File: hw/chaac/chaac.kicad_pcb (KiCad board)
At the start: 2 copper layers, 42 x 55 mm, 56 parts, among them J1 Battery, J2 TC2030-CTX, J3 UART, J4 windrain, Q1 Q_PMOS_GSD, SW1 RST, SW2 RST, U1 TPS7A0530PDBVT, U2 NRF52811-QFAA, U3 BMP280, U4 SHT3x-DIS, U5 E22-X00M22S, Y2 32.768kHz

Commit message: Adding chaac v5.0
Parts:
- removed the C14 at (117.5, 152.5)
- removed C16: 0.1uF, Capacitor_SMD:C_0603_1608Metric
- removed the R14 at (132.0, 168.0)
- removed the REF** at (124.4, 151.0)
- removed the REF** at (141.0, 133.0)
- removed the REF** at (107.0, 133.0)
- removed SW1, SW2: RST, alvarop:PTS820J25MSMTRLFS
- removed the U3 at (137.3, 146.0)
- added C2: 10uF, Resistor_SMD:R_0603_1608Metric, F.Cu at (116.6, 162.5)
- added C21: 0.1uF, Capacitor_SMD:C_0402_1005Metric, F.Cu at (141.2, 157.4)
- added C3: 4.7uF, Capacitor_SMD:C_0402_1005Metric, F.Cu at (119.6, 164.3)
- added C7: 0.1uF, Capacitor_SMD:C_0402_1005Metric, F.Cu at (142.0, 138.3)
- added C8: 4.7uF, Capacitor_SMD:C_0402_1005Metric, F.Cu at (122.8, 157.7)
- added D1: RB521CS30L,315, alvarop:RB521CS30L, F.Cu at (115.2, 168.7)
- added D2: LED_ALT, LED_SMD:LED_0603_1608Metric, F.Cu at (132.3, 159.7)
- added D3: LED_ALT, LED_SMD:LED_0603_1608Metric, F.Cu at (129.3, 159.7)
- added D4: LED_ALT, LED_SMD:LED_0603_1608Metric, F.Cu at (130.8, 159.7)
- added G***: LOGO, alvarop:weather_station, B.Cu at (115.0, 156.0)
- added J2: Battery, alvarop:S2B-PH-SM4-TB, F.Cu at (108.0, 142.0)
- added R1: 270k, Resistor_SMD:R_0402_1005Metric, F.Cu at (124.3, 165.2)
- added R10: 10k, Resistor_SMD:R_0402_1005Metric, F.Cu at (131.8, 164.2)
- added R11: 10k, Resistor_SMD:R_0402_1005Metric, F.Cu at (126.3, 165.7)
- added R12: 10k, Resistor_SMD:R_0402_1005Metric, F.Cu at (129.8, 164.2)
- added R13: 10k, Resistor_SMD:R_0402_1005Metric, F.Cu at (130.8, 164.2)
- added R20: 10k, Resistor_SMD:R_0402_1005Metric, F.Cu at (130.0, 171.3)
- added R4: 1M, Resistor_SMD:R_0402_1005Metric, F.Cu at (142.3, 167.1)
- added R5: 100k, Resistor_SMD:R_0402_1005Metric, F.Cu at (124.8, 157.7)
- added REF**: OSHW-Logo2_7.3x6mm_SilkScreen, Symbol:OSHW-Logo2_7.3x6mm_SilkScreen, F.Cu at (139.7, 151.9)
- added U2: MCP73871, alvarop:MCP73871, F.Cu at (124.8, 161.7)
- added U5: SHT3x-DIS, alvarop:SHT3x, F.Cu at (138.6, 157.4)
- C1: value 1uF -> 100uF; footprint Capacitor_SMD:C_0603_1608Metric -> Capacitor_SMD:CP_Elec_6.3x5.4
- C18: renamed from C17; footprint Capacitor_SMD:C_0603_1608Metric -> Capacitor_SMD:C_0402_1005Metric
- C19: renamed from C18; footprint Capacitor_SMD:C_0603_1608Metric -> Capacitor_SMD:C_0402_1005Metric
- C20: renamed from C15; footprint Capacitor_SMD:C_0603_1608Metric -> Capacitor_SMD:C_0402_1005Metric
- C22: renamed from C21; footprint Capacitor_SMD:C_0603_1608Metric -> Capacitor_SMD:C_0402_1005Metric
- C23: renamed from C22; footprint Capacitor_SMD:C_0603_1608Metric -> Capacitor_SMD:C_0402_1005Metric
- C24: renamed from C19; footprint Capacitor_SMD:C_0603_1608Metric -> Capacitor_SMD:C_0402_1005Metric
- C25: renamed from C20; footprint Capacitor_SMD:C_0603_1608Metric -> Capacitor_SMD:C_0402_1005Metric
- C5: renamed from C2; footprint Capacitor_SMD:C_0603_1608Metric -> Capacitor_SMD:C_0402_1005Metric
- C6: renamed from C7; footprint Capacitor_SMD:C_0603_1608Metric -> Capacitor_SMD:C_0402_1005Metric
- J1: value Battery -> Solar
- J3: footprint Connector_PinHeader_2.54mm:PinHeader_1x03_P2.54mm_Vertical -> Connector_PinHeader_2.54mm:PinHeader_1x02_P2.54mm_Vertical
- R14: renamed from R3; footprint Resistor_SMD:R_0603_1608Metric -> Resistor_SMD:R_0402_1005Metric
- R15: renamed from R4; footprint Resistor_SMD:R_0603_1608Metric -> Resistor_SMD:R_0402_1005Metric
- R16: renamed from R10; value 1k -> 0; footprint Resistor_SMD:R_0603_1608Metric -> Resistor_SMD:R_0402_1005Metric
- R17: renamed from R11; footprint Resistor_SMD:R_0603_1608Metric -> Resistor_SMD:R_0402_1005Metric
- R18: renamed from R12; footprint Resistor_SMD:R_0603_1608Metric -> Resistor_SMD:R_0402_1005Metric
- R19: renamed from R13; footprint Resistor_SMD:R_0603_1608Metric -> Resistor_SMD:R_0402_1005Metric
- R2: footprint Resistor_SMD:R_0603_1608Metric -> Resistor_SMD:R_0402_1005Metric
- R21: renamed from R5; footprint Resistor_SMD:R_0603_1608Metric -> Resistor_SMD:R_0402_1005Metric
- R22: renamed from R15; footprint Resistor_SMD:R_0603_1608Metric -> Resistor_SMD:R_0402_1005Metric
- R23: renamed from R16; footprint Resistor_SMD:R_0603_1608Metric -> Resistor_SMD:R_0402_1005Metric
- R3: renamed from R1; value 100k -> 1M; footprint Resistor_SMD:R_0603_1608Metric -> Resistor_SMD:R_0402_1005Metric
- R6, R7: value 4.7k -> 1M; footprint Resistor_SMD:R_0603_1608Metric -> Resistor_SMD:R_0402_1005Metric
- R8: value 0 -> 100k; footprint Resistor_SMD:R_0603_1608Metric -> Resistor_SMD:R_0402_1005Metric
- R9: value 0 -> 1M; footprint Resistor_SMD:R_0603_1608Metric -> Resistor_SMD:R_0402_1005Metric
- U4: value SHT3x-DIS -> DPS368; footprint alvarop:SHT3x -> alvarop:DPS368
- Y1: renamed from Y2; footprint Crystal:Crystal_SMD_3215-2Pin_3.2x1.5mm -> alvarop:ABS05
- moved J4 31.9 mm to (134.8, 131.7), turned to 180 degrees
- moved Q1 26.6 mm to (138.9, 167.9), turned to 0 degrees
- moved R21 21.3 mm to (136.4, 167.5), turned to 270 degrees
- moved U3 21.0 mm to (136.1, 139.3)
- moved R6 21.0 mm to (120.5, 155.2), turned to 90 degrees
- moved L2 20.8 mm to (137.9, 145.1)
- moved C17 20.7 mm to (138.8, 135.1)
- moved C14 20.6 mm to (131.5, 141.0), turned to 270 degrees
- moved C11 20.4 mm to (140.5, 143.0), turned to 90 degrees
- moved C10 20.2 mm to (139.5, 144.0), turned to 90 degrees
- moved Y1 20.1 mm to (141.5, 140.9), turned to 90 degrees
- moved C9 20.0 mm to (135.5, 145.7)
- moved L1 20.0 mm to (136.5, 145.7)
- moved C15 19.9 mm to (142.0, 139.4), turned to 0 degrees
- moved C12 19.6 mm to (132.0, 144.0), turned to 90 degrees
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- renumbered C4 to C10, C5 to C11, C6 to C12, C9 to C13, C11 to C14, C12 to C15, C13 to C17, C3 to C9, D1 to D5, D2 to D6, J2 to J4, J4 to J5, U2 to U3, U5 to U6
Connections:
- C1 pad 1: /VBATT -> /MCP_VIN
- C22 pad 1: Net-(C21-Pad1) -> +3V3
- C23 pad 1: Net-(C21-Pad1) -> +3V3
- J1 pad 2: /VBATT -> /SOLAR_IN
- J3 pad 2: /UART_RX -> /UART_TX
- R2 pad 1: GND -> Net-(R1-Pad2)
- R2 pad 2: /BATT -> GND
- R6 pad 1: /SCL -> GND
- R6 pad 2: +3V3 -> /BATT
- R7 pad 1: /SDA -> GND
- R7 pad 2: +3V3 -> /VSOLAR
- R8 pad 1: Net-(C21-Pad1) -> GND
- R8 pad 2: +3V3 -> Net-(R5-Pad2)
- R9 pad 1: Net-(C21-Pad1) -> GND
- R9 pad 2: /SNS_3V3 -> Net-(R9-Pad2)
- U1 pad 1: /VBATT -> /VIN
- U1 pad 3: /VBATT -> /VIN
- U3 pad 10: /SCL -> Net-(U3-Pad10)
- U3 pad 11: /UART_RX -> Net-(U3-Pad11)
- U3 pad 14: /E22_DIO1 -> Net-(U3-Pad14)
- U3 pad 15: /E22_BUSY -> Net-(U3-Pad15)
- U3 pad 16: /E22_NRST -> Net-(U3-Pad16)
- U3 pad 17: /MISO -> /E22_RXEN
- U3 pad 18: /MOSI -> /E22_TXEN
- U3 pad 19: /SCK -> /E22_DIO2
- U3 pad 21: /E22_RXEN -> /SCK
- U3 pad 22: /E22_TXEN -> /MOSI
- U3 pad 23: /E22_DIO2 -> /MISO
- U3 pad 27: /BOOT -> /E22_NRST
- U3 pad 28: Net-(U2-Pad28) -> /E22_BUSY
- U3 pad 29: Net-(U2-Pad29) -> /E22_DIO1
- U3 pad 37: /SNS_3V3_EN -> /LED2
- U3 pad 38: Net-(U2-Pad38) -> /LED1
- U3 pad 39: Net-(U2-Pad39) -> /SNS_3V3_EN
- U3 pad 7: /LED2 -> /VSOLAR
- U3 pad 8: /LED1 -> /SCL
- U4 pad 1: /SDA -> GND
- U4 pad 2: GND -> Net-(U4-Pad2)
- U4 pad 3: Net-(U4-Pad3) -> /SDA
- U4 pad 5: +3V3 -> GND
- U4 pad 6: Net-(U4-Pad6) -> +3V3
- U4 pad 8: GND -> +3V3
- U6 pad 9: Net-(C21-Pad1) -> +3V3
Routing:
- net /MCP_VIN: track 0.00 -> 66.8 mm
- net /SOLAR_IN: track 0.00 -> 61.5 mm
- net /VSOLAR: track 0.00 -> 36.6 mm, vias 0 -> 2
- net +3V3: track 169.0 -> 202.0 mm
- net /SNS_3V3: track 48.9 -> 22.7 mm, vias 4 -> 0
- net /UART_RX: track 24.3 -> 0.00 mm, vias 2 -> 0
- net /WSPEED: track 16.3 -> 39.2 mm
- net /SNS_3V3_EN: track 9.06 -> 30.0 mm, vias 0 -> 2
- net Net-(C21-Pad1): track 20.7 -> 0.00 mm
- net /BOOT: track 18.6 -> 0.00 mm, vias 2 -> 0
- net /SCL: track 50.6 -> 35.4 mm, vias 3 -> 0
- net /WDIR: track 20.6 -> 35.4 mm
- net /SDA: track 54.5 -> 40.2 mm, vias 3 -> 2
- net /UART_TX: track 19.9 -> 5.71 mm, vias 2 -> 0
- net /VIN: track 0.00 -> 13.2 mm
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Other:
- board text added: "4B"
- board text added: "SOLAR"
- board text added: "https://github.com/alvarop/chaac"
- board text added: "v5.0"
- board text removed: "(3-5.5V)"
- board text removed: "<--Temperature/Humidity"
- board text removed: "DFU"
- board text removed: "GND"
- board text removed: "Pressure"
- board text removed: "RST"
- board text removed: "RX"
- board text removed: "TX"
- board text removed: "https://github.com/alvarop/chaac/"
- board text removed: "v4.0"

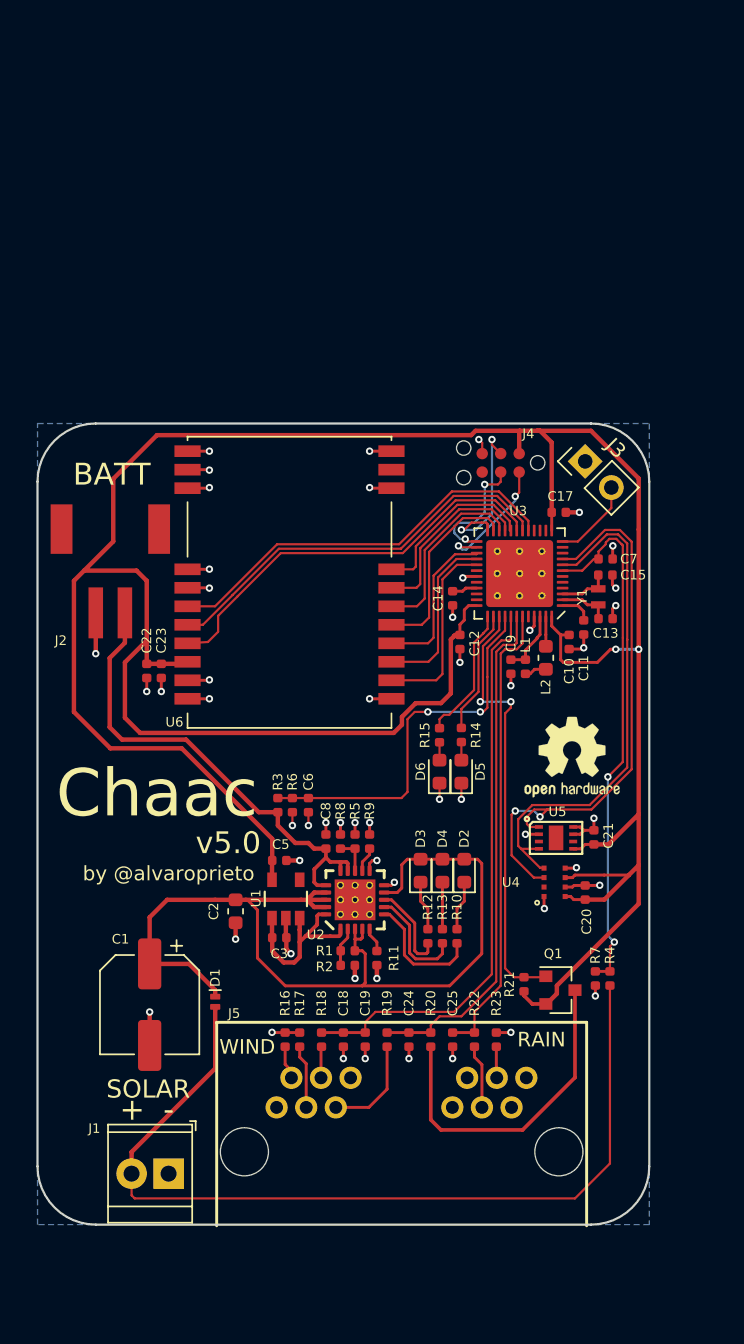
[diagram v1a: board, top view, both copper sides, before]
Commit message: Re-did layout for chaac v6
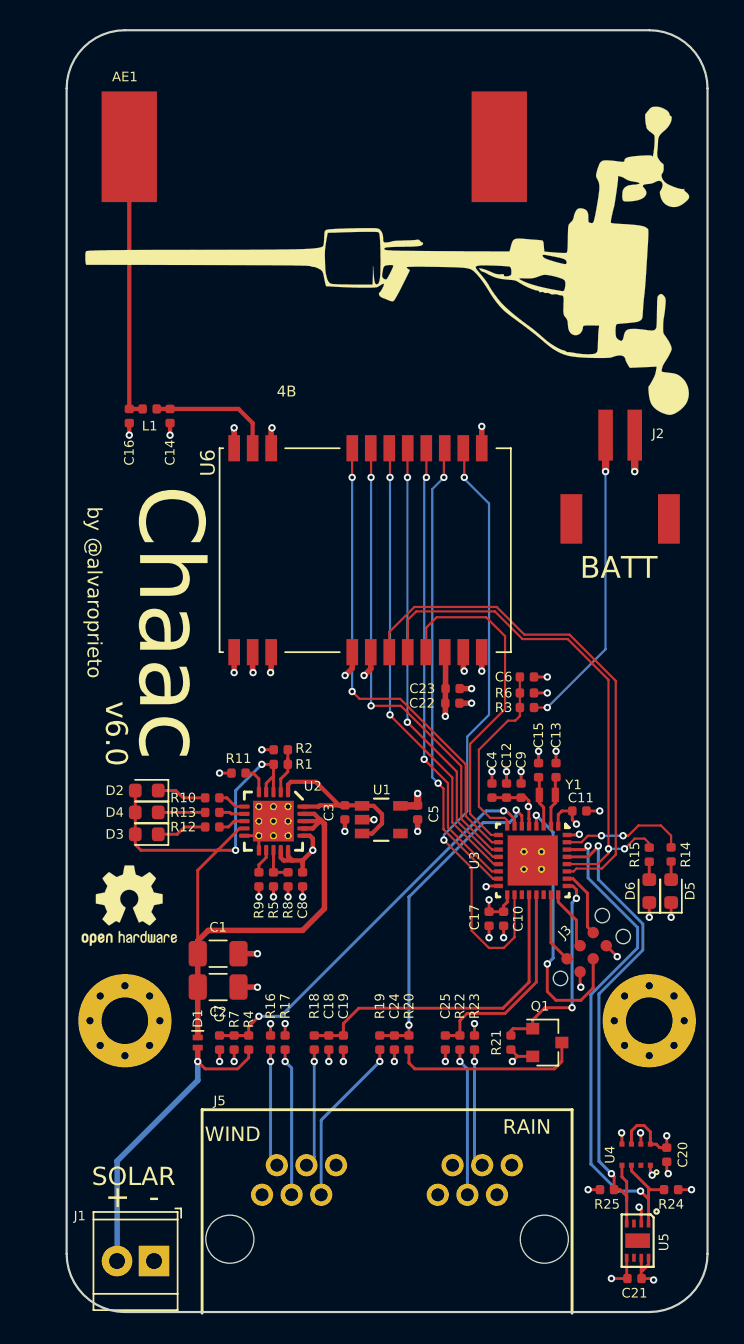
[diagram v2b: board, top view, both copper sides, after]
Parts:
- removed J4: TC2030-CTX, alvarop:TC2030-NL
- removed L2: 10uH, Inductor_SMD:L_0603_1608Metric
- added AE1: Antenna, alvarop:ANT-916-HESM, F.Cu at (122.0, 110.0)
- added C16: DNP, Capacitor_SMD:C_0402_1005Metric, F.Cu at (109.3, 128.5)
- added C4: 0.01 uF, Capacitor_SMD:C_0402_1005Metric, F.Cu at (134.2, 154.2)
- added G***: LOGO, alvarop:chaac_test_logo, B.Cu at (127.3, 118.0)
- added R24: 10k, Resistor_SMD:R_0402_1005Metric, F.Cu at (146.5, 181.6)
- added R25: 10k, Resistor_SMD:R_0402_1005Metric, F.Cu at (142.1, 181.6)
- added REF**: MountingHole_3.2mm_M3_Pad_Via, MountingHole:MountingHole_3.2mm_M3_Pad_Via, F.Cu at (145.0, 170.0)
- added REF**: MountingHole_3.2mm_M3_Pad_Via, MountingHole:MountingHole_3.2mm_M3_Pad_Via, F.Cu at (109.0, 170.0)
- C1: value 100uF -> 47uF; footprint Capacitor_SMD:CP_Elec_6.3x5.4 -> Capacitor_SMD:C_1206_3216Metric
- C14: value 100pF -> DNP
- C2: value 10uF -> 47uF; footprint Resistor_SMD:R_0603_1608Metric -> Capacitor_SMD:C_1206_3216Metric
- G***: moved to F.Cu
- J3: value UART -> TC2030-CTX; footprint Connector_PinHeader_2.54mm:PinHeader_1x02_P2.54mm_Vertical -> alvarop:TC2030-NL
- L1: value 15nH -> 0
- U3: value NRF52811-QFAA -> STM32L412K; footprint alvarop:NRF52811-QFN48-VIAS -> alvarop:UFQFPN32
- moved C7 42.5 mm to (115.5, 171.5), turned to 270 degrees
- moved G*** 40.0 mm to (127.2, 117.9), turned to 270 degrees
- moved J2 37.1 mm to (143.0, 129.8), turned to 180 degrees
- moved J3 33.7 mm to (140.7, 165.3)
- moved REF** 32.1 mm to (109.3, 162.1)
- moved L1 31.3 mm to (110.7, 128.0), turned to 180 degrees
- moved C21 30.4 mm to (144.0, 187.7), turned to 0 degrees
- moved C17 28.3 mm to (134.0, 163.0), turned to 90 degrees
- moved U5 28.2 mm to (144.2, 185.1), turned to 270 degrees
- moved R4 25.2 mm to (117.5, 171.5)
- moved R7 25.2 mm to (116.5, 171.5)
- moved C14 23.1 mm to (112.1, 128.5)
- moved D2 22.5 mm to (110.5, 154.2), turned to 180 degrees
- moved C22 21.1 mm to (131.5, 148.2), turned to 0 degrees
- moved D4 20.7 mm to (110.5, 155.7), turned to 180 degrees
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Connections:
- C11 pad 2: Net-(C11-Pad2) -> +3V3
- C9 pad 2: Net-(C9-Pad2) -> +3V3
- J3 pad 1: GND -> +3V3
- J3 pad 2: /UART_TX -> /SWDIO
- L1 pad 1: Net-(C9-Pad2) -> Net-(C14-Pad1)
- R15 pad 2: /LED2 -> /RADIO_TXEN
- U3 pad 1: Net-(C11-Pad2) -> +3V3
- U3 pad 10: Net-(U3-Pad10) -> /RADIO_CS
- U3 pad 11: Net-(U3-Pad11) -> /SCK
- U3 pad 12: /UART_TX -> /MISO
- U3 pad 13: +3V3 -> /MOSI
- U3 pad 14: Net-(U3-Pad14) -> /RADIO_NRST
- U3 pad 15: Net-(U3-Pad15) -> /RADIO_BUSY
- U3 pad 16: Net-(U3-Pad16) -> GND
- U3 pad 17: /E22_RXEN -> +3V3
- U3 pad 18: /E22_TXEN -> /RADIO_DIO1
- U3 pad 19: /E22_DIO2 -> Net-(U3-Pad19)
- U3 pad 20: /E22_NSS -> /WSPEED
- U3 pad 21: /SCK -> /RAIN
- U3 pad 22: /MOSI -> Net-(U3-Pad22)
- U3 pad 23: /MISO -> /SWDIO
- U3 pad 24: /nRST -> /SWCLK
- U3 pad 25: /SWDCLK -> /SNS_3V3_EN
- U3 pad 26: /SWDIO -> /SWO
- U3 pad 27: /E22_NRST -> /RADIO_RXEN
- U3 pad 28: /E22_BUSY -> /RADIO_TXEN
- U3 pad 29: /E22_DIO1 -> /SCL
- U3 pad 30: Net-(U3-Pad30) -> /SDA
- U3 pad 31: GND -> /LED1
- U3 pad 32: Net-(U3-Pad32) -> GND
- U3 pad 4: Net-(U3-Pad4) -> /NRST
- U3 pad 5: Net-(U3-Pad5) -> +3V3
- U3 pad 6: Net-(U3-Pad6) -> /WDIR
- U3 pad 8: /SCL -> /BATT
- U3 pad 9: /SDA -> /RADIO_DIO2
- U6 pad 13: /E22_DIO1 -> /RADIO_DIO1
- U6 pad 14: /E22_BUSY -> /RADIO_BUSY
- U6 pad 15: /E22_NRST -> /RADIO_NRST
- U6 pad 19: /E22_NSS -> /RADIO_CS
- U6 pad 21: Net-(U6-Pad21) -> Net-(C14-Pad1)
- U6 pad 6: /E22_RXEN -> /RADIO_RXEN
- U6 pad 7: /E22_TXEN -> /RADIO_TXEN
- U6 pad 8: /E22_DIO2 -> /RADIO_DIO2
- Y1 pad 1: Net-(C13-Pad1) -> Net-(C15-Pad1)
- Y1 pad 2: Net-(C15-Pad1) -> Net-(C13-Pad1)
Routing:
- net +3V3: track 202.0 -> 30.0 mm, vias 2 -> 11
- net /RADIO_DIO1: track 0.00 -> 42.6 mm, vias 0 -> 2
- net /SOLAR_IN: track 61.5 -> 21.5 mm, vias 0 -> 1
- net /RADIO_TXEN: track 0.00 -> 37.1 mm, vias 0 -> 2
- net /VBATT: track 33.5 -> 69.2 mm, vias 0 -> 3
- net /RADIO_RXEN: track 0.00 -> 35.5 mm
- net /RADIO_CS: track 0.00 -> 33.1 mm, vias 0 -> 2
- net /RADIO_BUSY: track 0.00 -> 32.0 mm, vias 0 -> 2
- net /RADIO_NRST: track 0.00 -> 31.5 mm, vias 0 -> 2
- net /E22_DIO2: track 28.5 -> 0.00 mm
- net /E22_RXEN: track 28.2 -> 0.00 mm
- net /E22_TXEN: track 28.0 -> 0.00 mm
- net /RADIO_DIO2: track 0.00 -> 23.7 mm
- net /SCK: track 12.4 -> 32.6 mm, vias 0 -> 2
- net /NRST: track 0.00 -> 19.2 mm, vias 0 -> 2
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- added copper zone on PWR.Cu, net +3V3
- added copper zone on GND.Cu, net GND
- removed copper zone on B.Cu, net GND
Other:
- board size 42 x 55 mm -> 44 x 88 mm
- copper layers 2 -> 4
- board text added: "v6.0"
- board text removed: "v5.0"

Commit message: Cleaned up chaac layout
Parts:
- removed the G*** at (127.3, 118.0)
- removed the REF** at (145.0, 170.0)
- removed the REF** at (109.0, 170.0)
- added G***: LOGO, alvarop:weather_station_tiny, F.Cu at (144.5, 149.0)
- added REF**: MountingHole_3.2mm_M3, MountingHole:MountingHole_3.2mm_M3, F.Cu at (145.0, 170.0)
- added REF**: MountingHole_3.2mm_M3, MountingHole:MountingHole_3.2mm_M3, F.Cu at (109.0, 170.0)
- G***: moved to B.Cu
- U3: footprint alvarop:UFQFPN32 -> alvarop:UFQFPN32_ALT
- moved G*** 20.6 mm to (128.0, 138.5), turned to 180 degrees
- moved REF** 18.2 mm to (127.5, 163.0)
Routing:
- net GND: vias 56 -> 65
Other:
- board size 44 x 88 mm -> 44 x 85 mm
- board text added: "chaac.network"
- board text added: "github.com/alvarop/chaac"
- board text removed: "https://chaac.network"
- board text removed: "https://github.com/alvarop/chaac"
